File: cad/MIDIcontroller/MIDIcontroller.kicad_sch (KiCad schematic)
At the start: 1 part

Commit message: Started routing
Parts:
- added H1, H2, H3, H4: MountingHole, MountingHole:MountingHole_4.3mm_M4, symbol Mechanical:MountingHole
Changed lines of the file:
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@@
+    )
+  )
+  (symbol (lib_id "Mechanical:MountingHole") (at 120.65 124.46 0) (unit 1)
+    (in_bom yes) (on_board yes) (fields_autoplaced)
+    (property "Reference" "H2" (id 0) (at 123.19 123.1899 0)
+      (effects (font (size 1.27 1.27)) (justify left))
+    )
+    (property "Value" "MountingHole" (id 1) (at 123.19 125.7299 0)
+      (effects (font (size 1.27 1.27)) (justify left))
+    )
+    (property "Footprint" "MountingHole:MountingHole_4.3mm_M4" (id 2) (at 120.65 124.46 0)
+      (effects (font (size 1.27 1.27)) hide)
+    )
+    (property "Datasheet" "~" (id 3) (at 120.65 124.46 0)
+      (effects (font (size 1.27 1.27)) hide)
+    )
+  )
+  (symbol (lib_id "Mechanical:MountingHole") (at 99.06 132.08 0) (unit 1)
+    (in_bom yes) (on_board yes) (fields_autoplaced)
+    (property "Reference" "H3" (id 0) (at 101.6 130.8099 0)
+      (effects (font (size 1.27 1.27)) (justify left))
+    )
+    (property "Value" "MountingHole" (id 1) (at 101.6 133.3499 0)
+      (effects (font (size 1.27 1.27)) (justify left))
+    )
+    (property "Footprint" "MountingHole:MountingHole_4.3mm_M4" (id 2) (at 99.06 132.08 0)
+      (effects (font (size 1.27 1.27)) hide)
+    )
+    (property "Datasheet" "~" (id 3) (at 99.06 132.08 0)
+      (effects (font (size 1.27 1.27)) hide)
     )
   )
@@
     (pin "9")
   )
+  (symbol (lib_id "Mechanical:MountingHole") (at 120.65 132.08 0) (unit 1)
+    (in_bom yes) (on_board yes) (fields_autoplaced)
+    (property "Reference" "H4" (id 0) (at 123.19 130.8099 0)
+      (effects (font (size 1.27 1.27)) (justify left))
+    )
+    (property "Value" "MountingHole" (id 1) (at 123.19 133.3499 0)
+      (effects (font (size 1.27 1.27)) (justify left))
+    )
+    (property "Footprint" "MountingHole:MountingHole_4.3mm_M4" (id 2) (at 120.65 132.08 0)
+      (effects (font (size 1.27 1.27)) hide)
+    )
+    (property "Datasheet" "~" (id 3) (at 120.65 132.08 0)
+      (effects (font (size 1.27 1.27)) hide)
+    )
+  )
+  (symbol (lib_id "Mechanical:MountingHole") (at 99.06 124.46 0) (unit 1)
+    (in_bom yes) (on_board yes) (fields_autoplaced)
+    (property "Reference" "H1" (id 0) (at 101.6 123.1899 0)
+      (effects (font (size 1.27 1.27)) (justify left))
+    )
+    (property "Value" "MountingHole" (id 1) (at 101.6 125.7299 0)
+      (effects (font (size 1.27 1.27)) (justify left))
+    )
+    (property "Footprint" "MountingHole:MountingHole_4.3mm_M4" (id 2) (at 99.06 124.46 0)
+      (effects (font (size 1.27 1.27)) hide)
+    )
+    (property "Datasheet" "~" (id 3) (at 99.06 124.46 0)
+      (effects (font (size 1.27 1.27)) hide)
+    )
+  )
   (sheet (at 93.98 73.66) (size 21.59 15.24) (fields_autoplaced)
     (stroke (width 0.1524) (type solid) (color 0 0 0 0))
@@
       (reference "D_SW4") (unit 1) (value "LED") (footprint "LED_SMD:LED_1206_3216Metric")
     )
+    (path "/b555bffd-44b2-46a0-b0cf-743a5afe890a"
+      (reference "H1") (unit 1) (value "MountingHole") (footprint "MountingHole:MountingHole_4.3mm_M4")
+    )
+    (path "/66e388e7-84a5-4887-918b-19ac4a643322"
+      (reference "H2") (unit 1) (value "MountingHole") (footprint "MountingHole:MountingHole_4.3mm_M4")
+    )
+    (path "/6711a69f-6a34-4672-a897-01cc045485fc"
+      (reference "H3") (unit 1) (value "MountingHole") (footprint "MountingHole:MountingHole_4.3mm_M4")
+    )
+    (path "/95361b97-0c47-4a93-8f8f-57af6feefa0d"
+      (reference "H4") (unit 1) (value "MountingHole") (footprint "MountingHole:MountingHole_4.3mm_M4")
+    )
     (path "/c26d15d9-372b-4fcf-8414-83869c4ab44e/4ae7fd2e-e09f-435f-ad7f-916187916c6b"

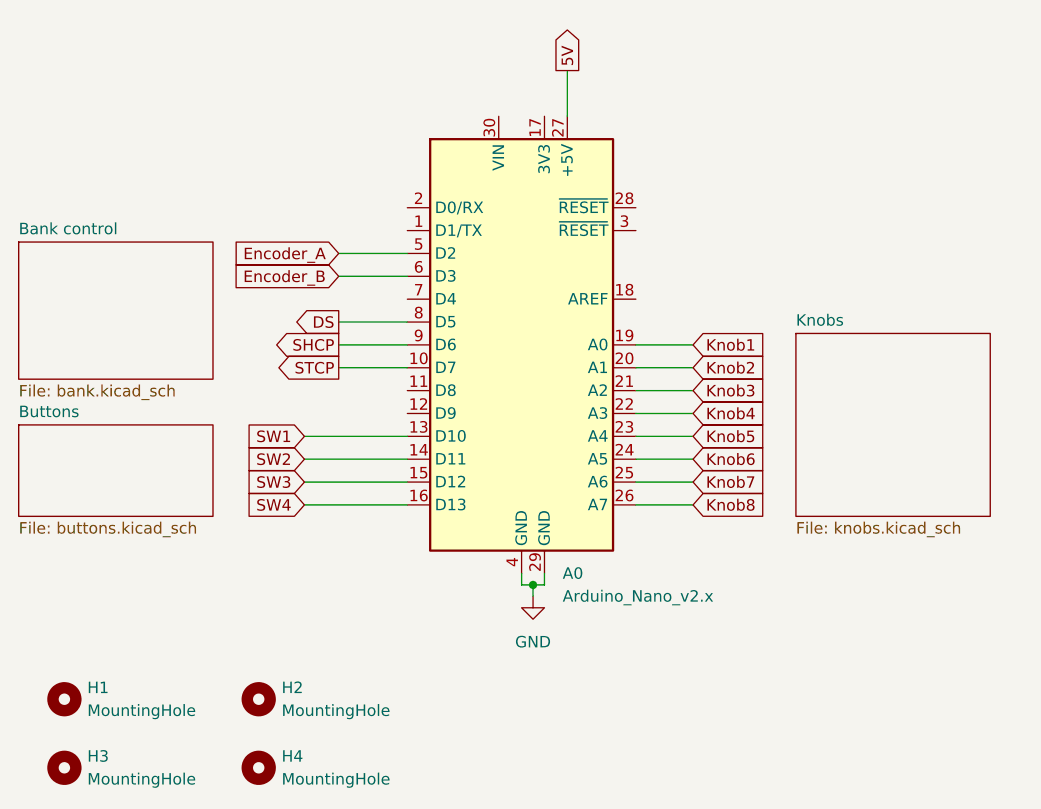
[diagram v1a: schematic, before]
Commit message: Added button on encoder
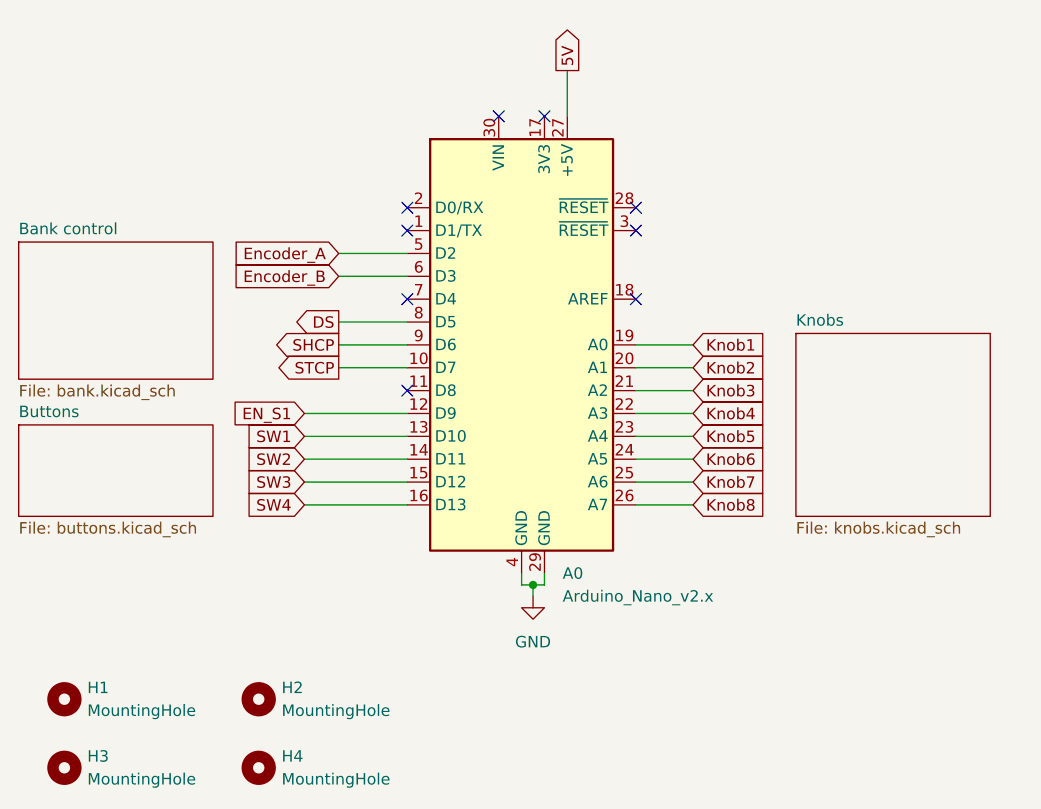
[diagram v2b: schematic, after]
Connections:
- net EN_S1: now reaches A0.12 (D9)
- no-connect marks 0 -> 9
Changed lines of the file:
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@@
   (junction (at 151.13 111.76) (diameter 0) (color 0 0 0 0)
   )
+  (no_connect (at 162.56 69.85))
+  (no_connect (at 152.4 59.69))
+  (no_connect (at 137.16 72.39))
+  (no_connect (at 137.16 80.01))
+  (no_connect (at 147.32 59.69))
+  (no_connect (at 137.16 69.85))
+  (no_connect (at 162.56 72.39))
+  (no_connect (at 162.56 80.01))
+  (no_connect (at 137.16 90.17))
   (wire (pts (xy 149.86 111.76) (xy 151.13 111.76))
     (stroke (width 0) (type default) (color 0 0 0 0))
@@
     (stroke (width 0) (type default) (color 0 0 0 0))
   )
+  (wire (pts (xy 125.73 92.71) (xy 137.16 92.71))
+    (stroke (width 0) (type default) (color 0 0 0 0))
+  )
   (wire (pts (xy 125.73 100.33) (xy 137.16 100.33))
     (stroke (width 0) (type default) (color 0 0 0 0))
@@
     (effects (font (size 1.27 1.27)) (justify right))
     (property "Riferimenti inter-foglio" "${INTERSHEET_REFS}" (id 0) (at 119.4464 95.1706 0)
+      (effects (font (size 1.27 1.27)) (justify right) hide)
+    )
+  )
+  (global_label "EN_S1" (shape input) (at 125.73 92.71 180) (fields_autoplaced)
+    (effects (font (size 1.27 1.27)) (justify right))
+    (property "Riferimenti inter-foglio" "${INTERSHEET_REFS}" (id 0) (at 117.4507 92.6306 0)
       (effects (font (size 1.27 1.27)) (justify right) hide)
     )
@@
       (reference "#PWR0118") (unit 1) (value "GND") (footprint "")
     )
+    (path "/20a291b4-c404-4138-ad99-1a2e5671a6b2/6b5f8795-0033-4ede-a14f-98318d4c48a1"
+      (reference "#PWR0119") (unit 1) (value "GND") (footprint "")
+    )
     (path "/884b9d54-80ae-4e54-a815-6e293bda6859"
       (reference "A0") (unit 1) (value "Arduino_Nano_v2.x") (footprint "Module:Arduino_Nano")
@@
       (reference "C_ENB1") (unit 1) (value "10n") (footprint "Capacitor_Tantalum_SMD:CP_EIA-1608-08_AVX-J")
     )
+    (path "/20a291b4-c404-4138-ad99-1a2e5671a6b2/5b09d0cb-8d06-4f27-8e82-18f666e53b19"
+      (reference "C_ENSW1") (unit 1) (value "220n") (footprint "Capacitor_Tantalum_SMD:CP_EIA-1608-08_AVX-J")
+    )
     (path "/e72fcb59-f9ff-4380-bc76-0e706ee9ae8d/ee8a2ba9-5028-445b-8834-7e18569ef9cf"
       (reference "C_SW1") (unit 1) (value "220n") (footprint "Capacitor_Tantalum_SMD:CP_EIA-1608-08_AVX-J")
@@
       (reference "R_ENB2") (unit 1) (value "10k") (footprint "Resistor_SMD:R_0805_2012Metric")
     )
+    (path "/20a291b4-c404-4138-ad99-1a2e5671a6b2/9074d8cb-d7a2-4dff-ac33-64bbd248877f"
+      (reference "R_ENSW1") (unit 1) (value "10k") (footprint "Resistor_SMD:R_0805_2012Metric")
+    )
     (path "/e72fcb59-f9ff-4380-bc76-0e706ee9ae8d/9ec1567d-4aeb-4c4a-bffe-3b0fff8e802f"
       (reference "R_SW1") (unit 1) (value "330") (footprint "Resistor_SMD:R_0805_2012Metric")
@@
       (reference "R_SW4") (unit 1) (value "330") (footprint "Resistor_SMD:R_0805_2012Metric")
     )
-    (path "/e72fcb59-f9ff-4380-bc76-0e706ee9ae8d/237008f9-b98d-4399-95ce-779f5d1c301f"
-      (reference "SW1") (unit 1) (value "SW_SPST") (footprint "Button_Switch_THT:SW_SPST_Omron_B3F-315x_Angled")
-    )
-    (path "/e72fcb59-f9ff-4380-bc76-0e706ee9ae8d/940f1bbb-4a93-4e6e-9666-3816ac43a755"
-      (reference "SW2") (unit 1) (value "SW_SPST") (footprint "Button_Switch_THT:SW_SPST_Omron_B3F-315x_Angled")
-    )
-    (path "/e72fcb59-f9ff-4380-bc76-0e706ee9ae8d/025e7e44-d9e2-4837-811e-ea33436f9fb9"
-      (reference "SW3") (unit 1) (value "SW_SPST") (footprint "Button_Switch_THT:SW_SPST_Omron_B3F-315x_Angled")
-    )
-    (path "/e72fcb59-f9ff-4380-bc76-0e706ee9ae8d/b0c16084-2ae6-494a-b845-9147b687876a"
-      (reference "SW4") (unit 1) (value "SW_SPST") (footprint "Button_Switch_THT:SW_SPST_Omron_B3F-315x_Angled")
+    (path "/e72fcb59-f9ff-4380-bc76-0e706ee9ae8d/42ac24b0-e15b-4a02-ae76-9b444669c7a9"
+      (reference "SW1") (unit 1) (value "SW_Push_Dual") (footprint "Button_Switch_THT:SW_PUSH_6mm_H5mm")
+    )
+    (path "/e72fcb59-f9ff-4380-bc76-0e706ee9ae8d/049a6df3-7fc0-4998-8a9b-108be31f7d02"
+      (reference "SW2") (unit 1) (value "SW_Push_Dual") (footprint "Button_Switch_THT:SW_PUSH_6mm_H5mm")
+    )
+    (path "/e72fcb59-f9ff-4380-bc76-0e706ee9ae8d/729b79c9-0d4a-4104-ac87-61607b4cd4e6"
+      (reference "SW3") (unit 1) (value "SW_Push_Dual") (footprint "Button_Switch_THT:SW_PUSH_6mm_H5mm")
+    )
+    (path "/e72fcb59-f9ff-4380-bc76-0e706ee9ae8d/1e84c12f-2137-461f-9820-c08fd35a559f"
+      (reference "SW4") (unit 1) (value "SW_Push_Dual") (footprint "Button_Switch_THT:SW_PUSH_6mm_H5mm")
     )
     (path "/20a291b4-c404-4138-ad99-1a2e5671a6b2/79dabf10-e82d-4f0a-b798-52d25adfbdf1"
